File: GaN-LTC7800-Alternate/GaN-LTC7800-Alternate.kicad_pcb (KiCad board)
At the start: 2 copper layers, 40 parts, among them Q1 EPC2014C, Q2 EPC2014C, U1 LTC7800HUDC_PBF

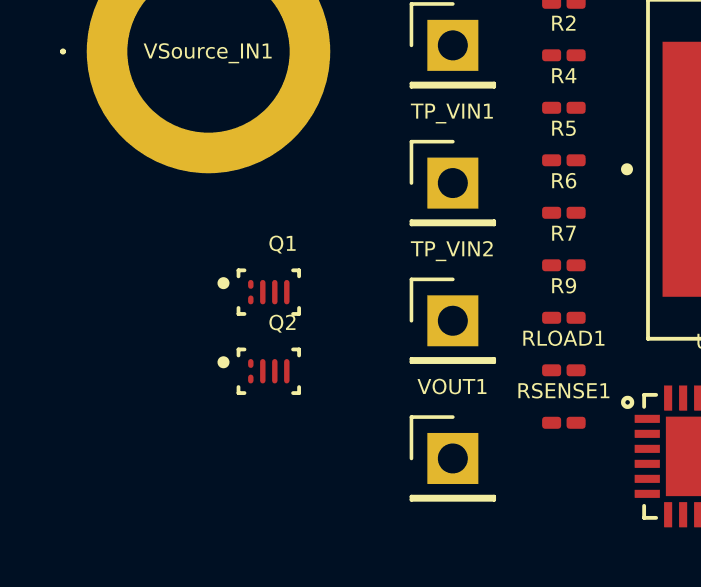
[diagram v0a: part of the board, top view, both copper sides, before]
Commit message: new GaN switches, added alt projects
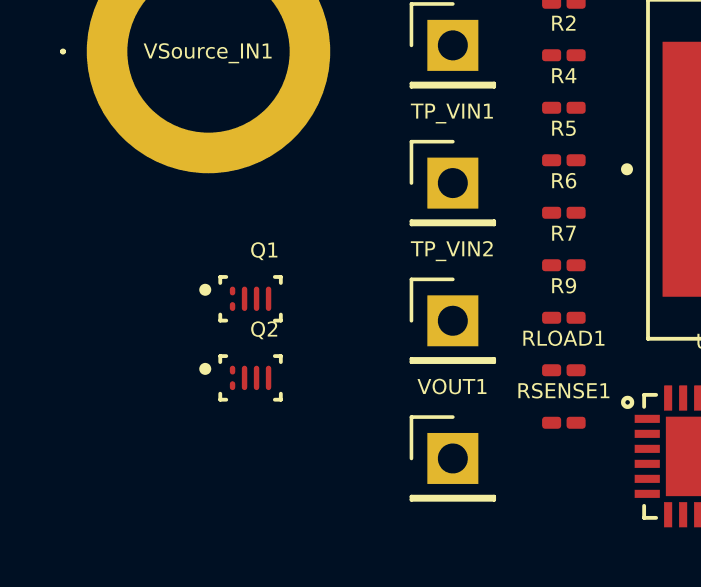
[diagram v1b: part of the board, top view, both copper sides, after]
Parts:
- moved Q1 0.65 mm to (82.4, 133.8)
- moved Q2 0.65 mm to (82.4, 136.4)

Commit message: alternates
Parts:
- C2, C2_EX1, D1, R1: moved to B.Cu
- moved Q2 110.3 mm to (145.5, 45.9)
- moved Q1 105.7 mm to (145.5, 49.0), turned to 180 degrees
- moved VOUT1 96.3 mm to (116.5, 46.8)
- moved D1 87.9 mm to (91.3, 50.8)
- moved RLOAD1 87.2 mm to (121.2, 53.8)
- moved RSENSE1 86.7 mm to (115.5, 54.2)
- moved U1 81.4 mm to (92.5, 57.8), turned to 90 degrees
- moved R4 74.2 mm to (115.5, 56.8)
- moved L1 73.2 mm to (108.5, 56.8)
- moved R7 72.9 mm to (123.3, 66.5), turned to 180 degrees
- moved GND1 72.7 mm to (126.0, 62.8)
- moved R6 72.6 mm to (121.5, 64.2)
- moved R5 69.0 mm to (121.0, 66.2), turned to -90 degrees
- moved R1 68.5 mm to (96.2, 55.5), turned to 90 degrees
- moved R9 68.3 mm to (88.5, 66.2), turned to 180 degrees
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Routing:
- net /VIN: track 0.00 -> 82.0 mm, vias 0 -> 2
- net /TG: track 0.00 -> 69.7 mm, vias 0 -> 2
- net /SW: track 0.00 -> 66.1 mm
- net /BG: track 0.00 -> 61.5 mm, vias 0 -> 2
- net /VFB: track 0.00 -> 31.9 mm, vias 0 -> 2
- net /Vout: track 0.00 -> 31.5 mm, vias 0 -> 90
- net /SENSE+: track 0.00 -> 21.9 mm, vias 0 -> 2
- net /INTVCC: track 0.00 -> 18.0 mm, vias 0 -> 1
- net /ITH: track 0.00 -> 13.6 mm, vias 0 -> 2
- net /BOOST: track 0.00 -> 13.2 mm, vias 0 -> 2
- net Net-(U1-FREQ): track 0.00 -> 10.2 mm
- net Net-(U1-TRACK/SS): track 0.00 -> 9.83 mm
- net GND: track 0.00 -> 5.12 mm, vias 0 -> 36
- net Net-(C5-Pad2): track 0.00 -> 5.01 mm
- net Net-(U1-PGOOD): track 0.00 -> 4.10 mm, vias 0 -> 1
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- added copper zone on B.Cu, net GND
- added copper zone on F.Cu, net GND
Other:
- board outline added: 86.2 x 46.5 mm

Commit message: alternates good
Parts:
- moved VSource_GND1 3.75 mm to (111.0, 78.0)
- moved TP_VIN2 2.50 mm to (118.8, 80.2)
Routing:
- net /BG: track 61.5 -> 57.9 mm
- net /VIN: track 82.0 -> 79.1 mm
- net /SW: track 66.1 -> 68.9 mm
- net GND: vias 36 -> 58
